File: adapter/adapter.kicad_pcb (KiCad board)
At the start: 2 copper layers, 41.8 x 50.8 mm, 28 parts, among them J1 Serial, J2 Battery charge, J3 Ribbon, J4 Ribbon, J5 RGB, SW1 SW_SPST, SW3 SW_SPDT, U1 Dual MCU: RP2040 + nice!nano, U2 AP1603WG-7, U3 USBLC6-2P6

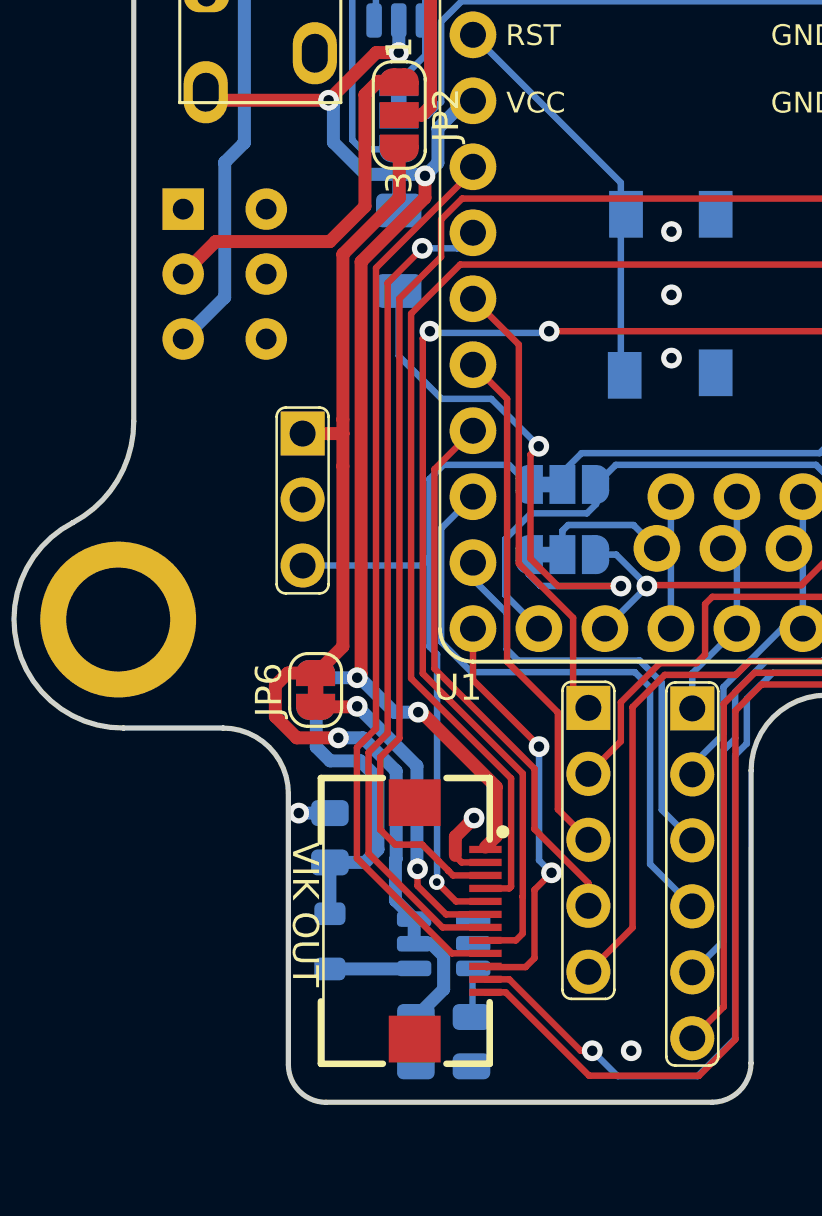
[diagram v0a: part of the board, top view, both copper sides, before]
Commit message: pcb: update silk screen to have text
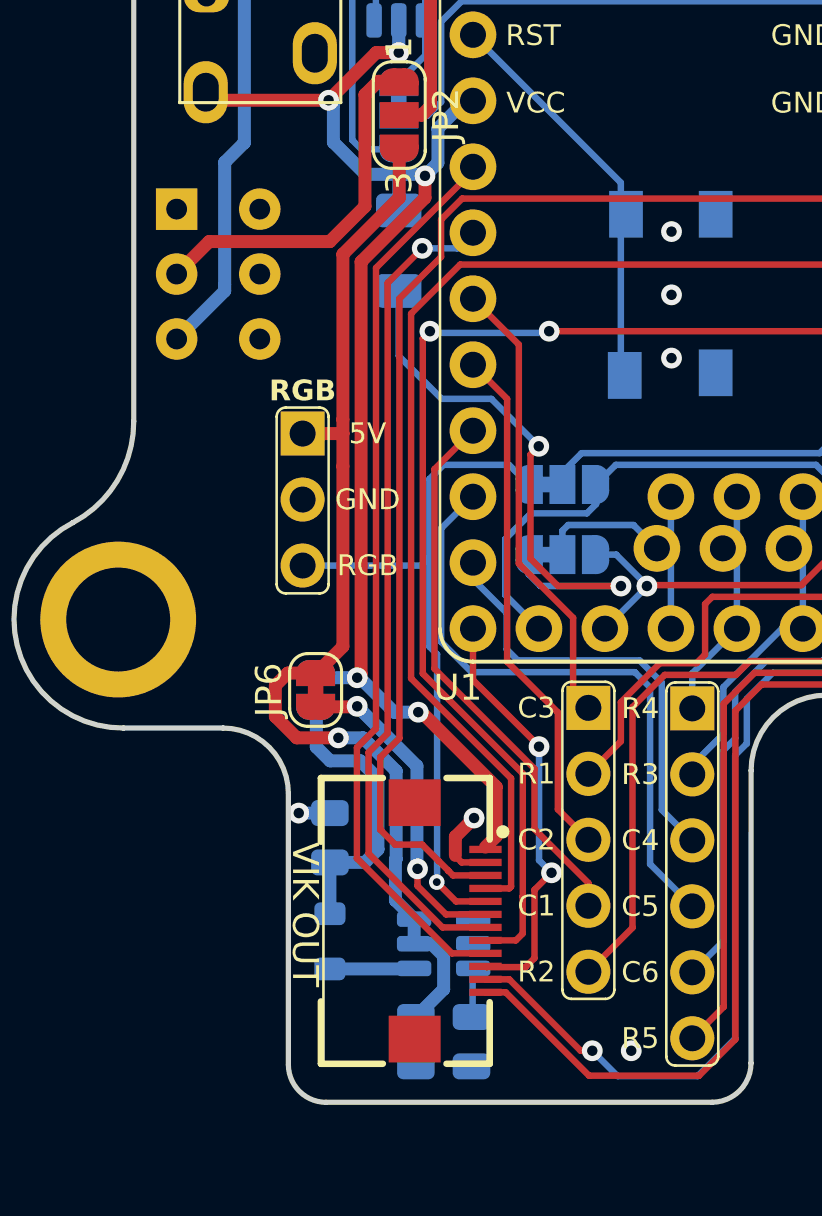
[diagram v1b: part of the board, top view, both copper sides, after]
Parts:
- moved SW3 0.25 mm to (119.2, 83.6)
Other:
- board text removed: "5V"
- board text removed: "DIN"
- board text removed: "GND"

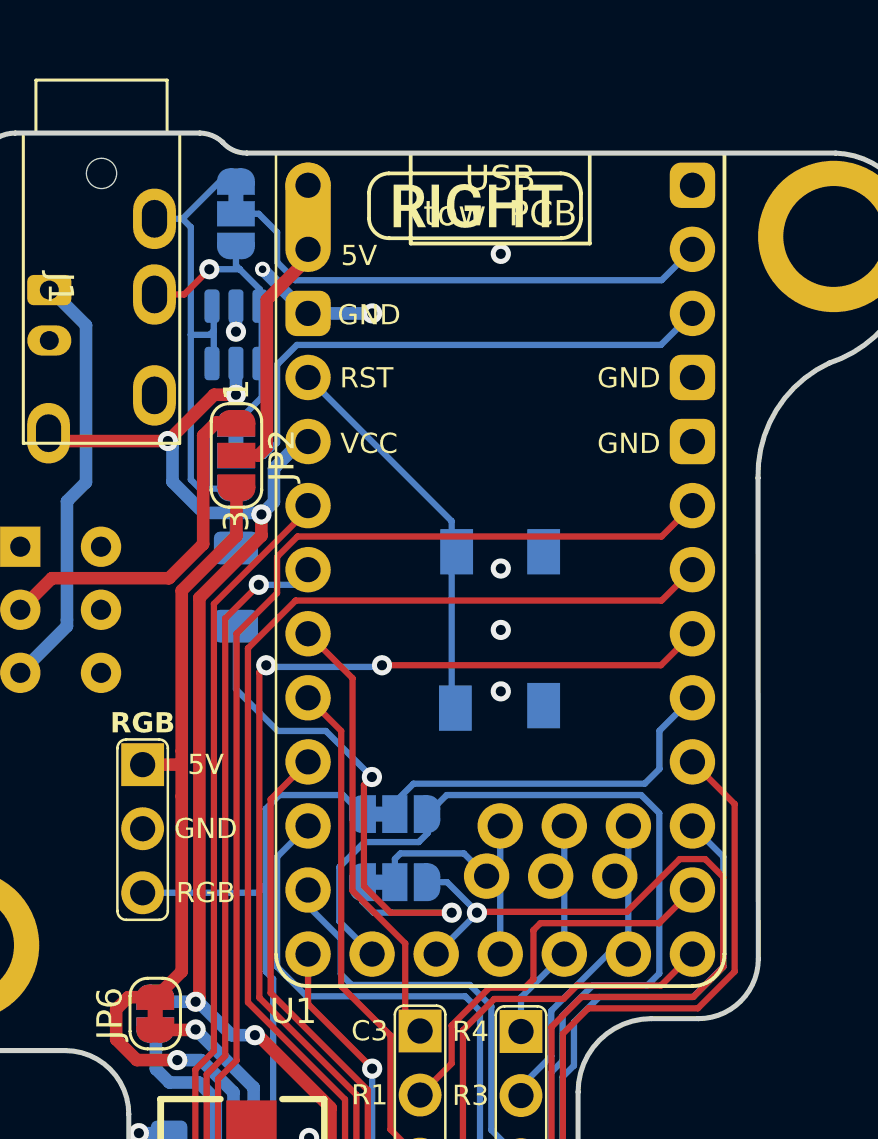
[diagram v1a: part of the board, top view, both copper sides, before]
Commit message: pcb: update silk screen on mcus
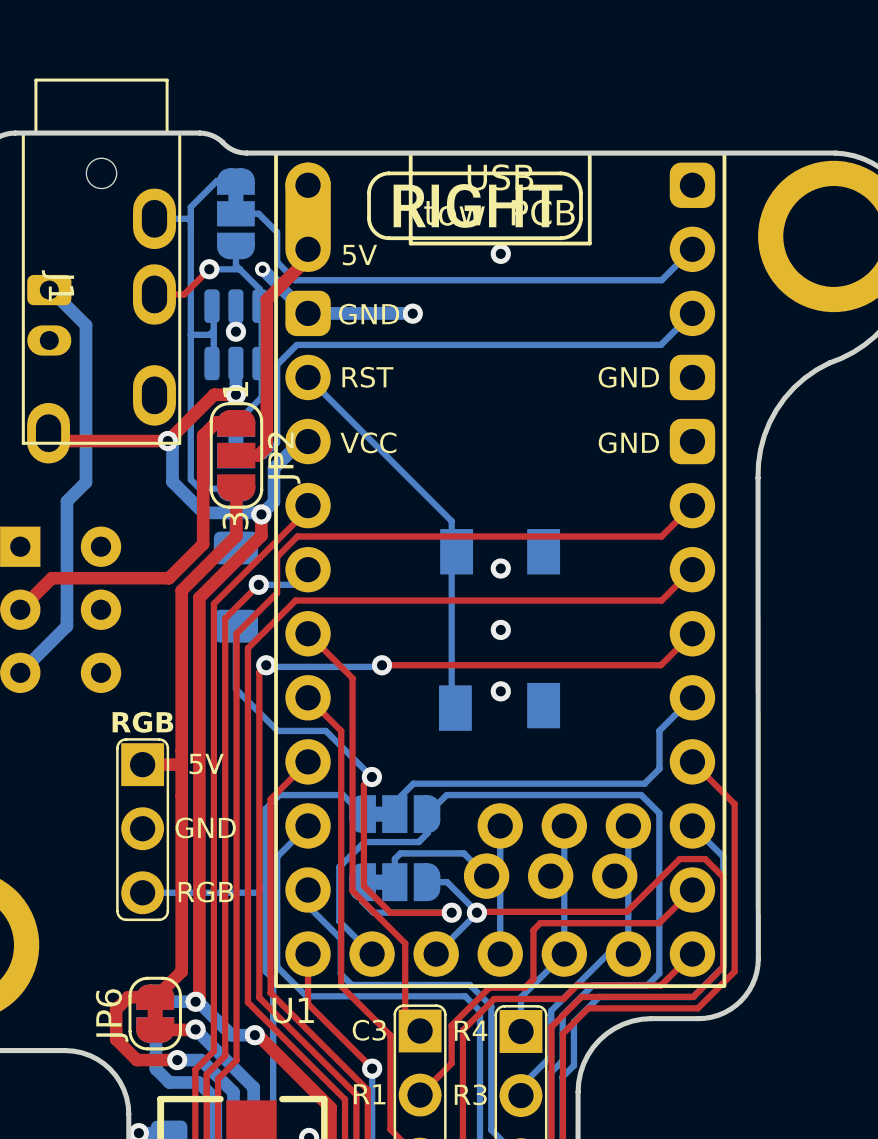
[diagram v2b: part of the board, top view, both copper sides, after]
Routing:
- net GND_L: track 10.3 -> 12.0 mm
- net TX_L: track 19.1 -> 19.9 mm

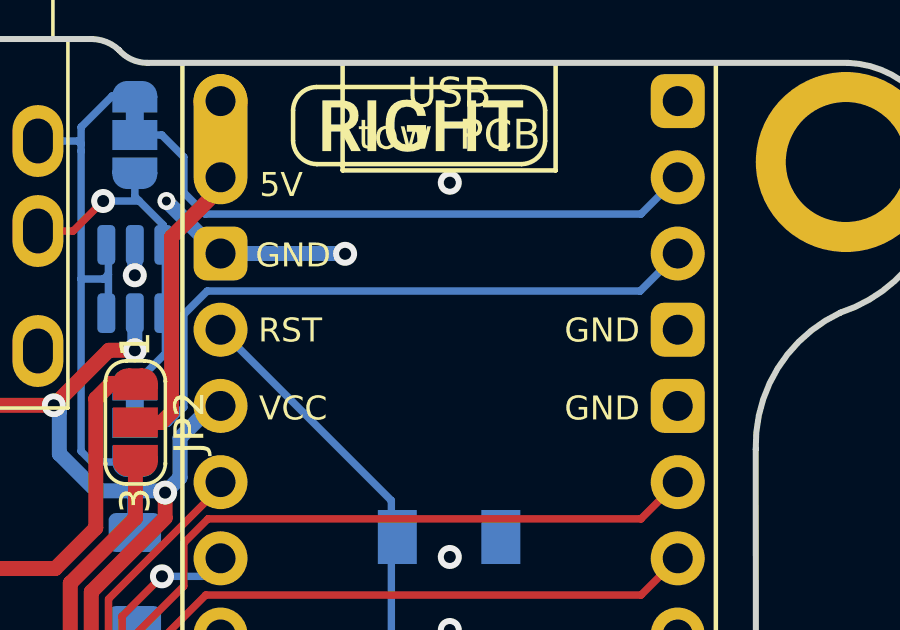
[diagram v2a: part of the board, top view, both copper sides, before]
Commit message: pcb: add osh silk screen
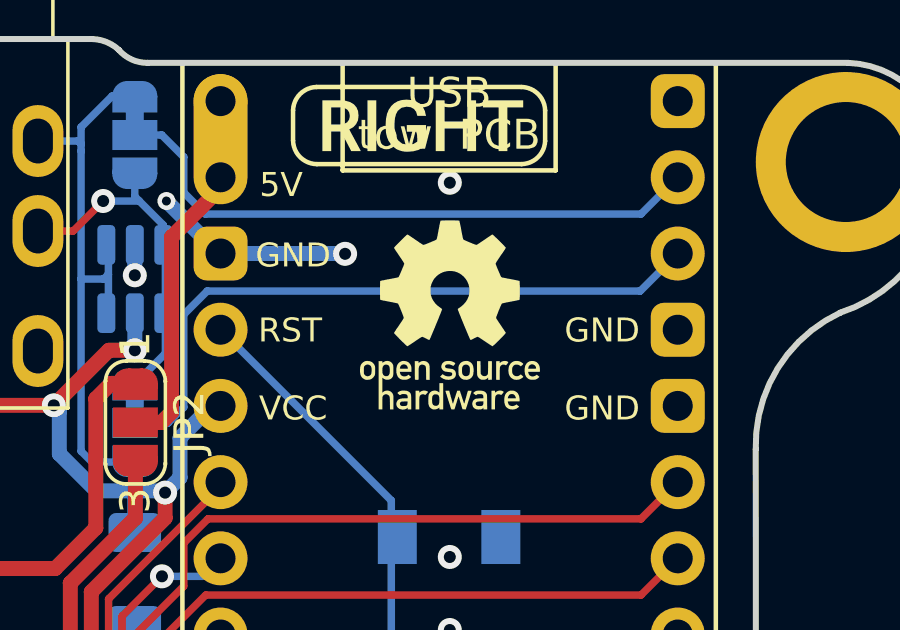
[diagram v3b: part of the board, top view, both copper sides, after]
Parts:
- added G***: LOGO, LOGO, F.Cu at (138.2, 76.4)
- added G***: LOGO, LOGO, B.Cu at (138.2, 76.4)

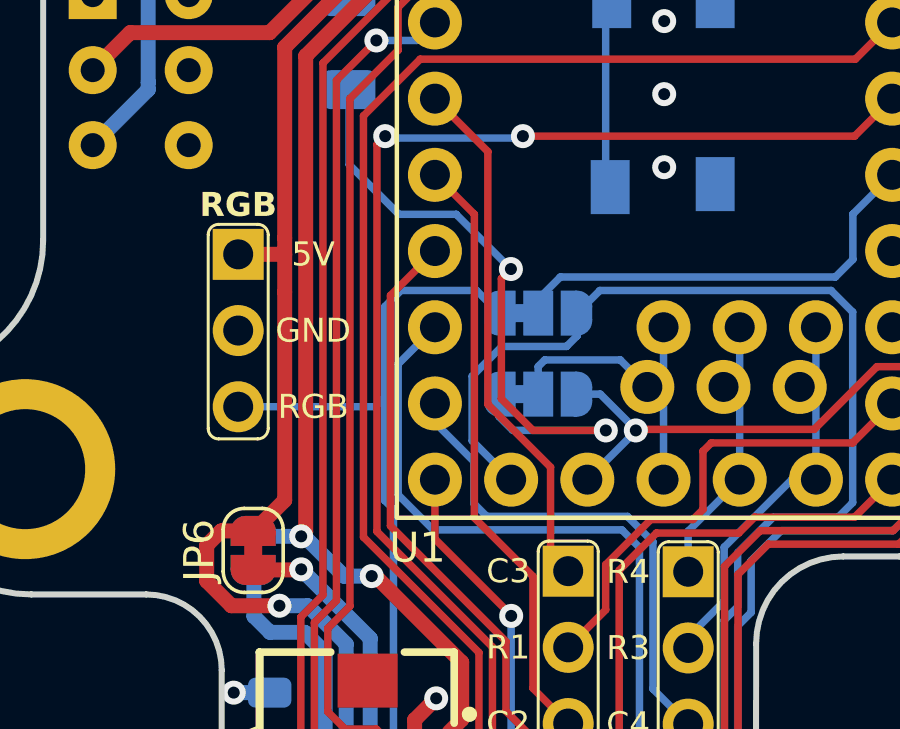
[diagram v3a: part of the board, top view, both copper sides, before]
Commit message: pcb: add more sikscreen
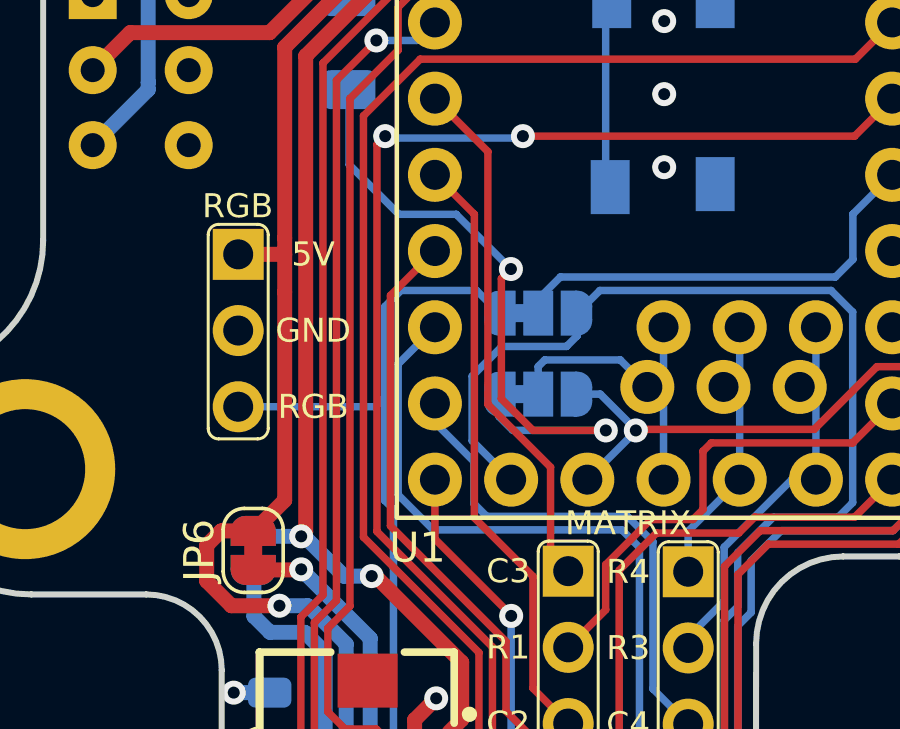
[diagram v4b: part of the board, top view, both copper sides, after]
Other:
- board text added: "MATRIX"

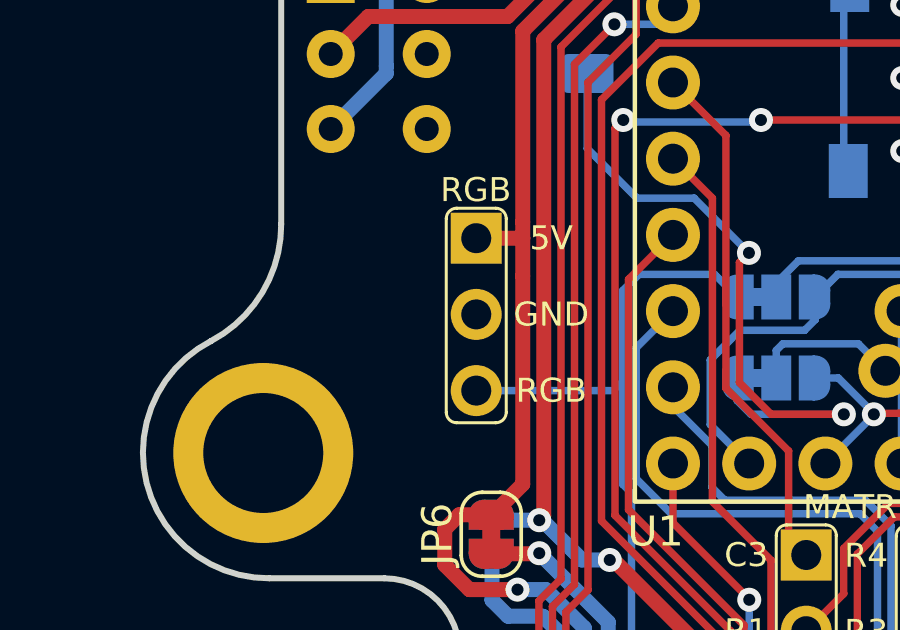
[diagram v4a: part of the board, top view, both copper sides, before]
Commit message: pcb: fix drc
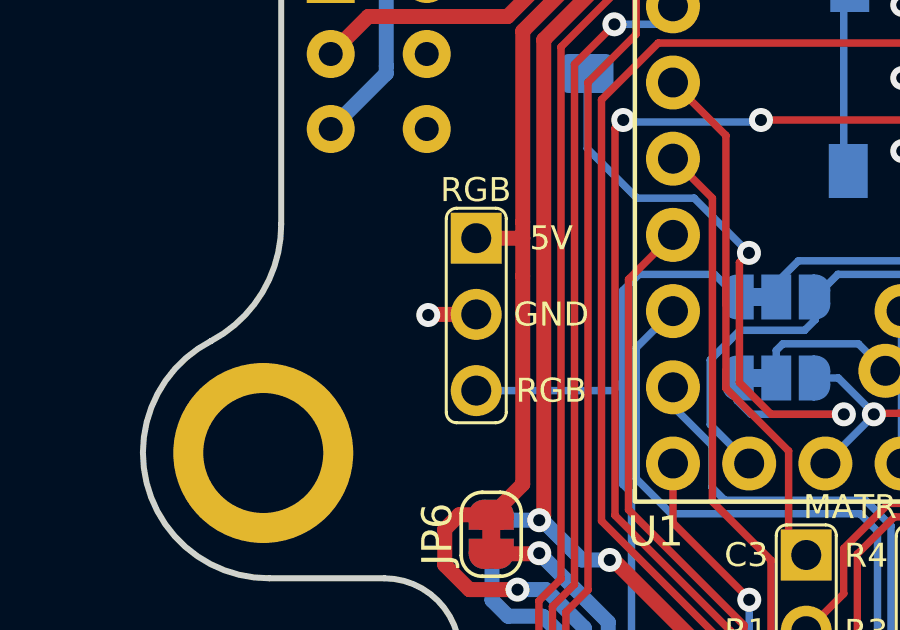
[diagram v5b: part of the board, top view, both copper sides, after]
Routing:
- net GND_L: track 12.0 -> 13.6 mm, vias 10 -> 11
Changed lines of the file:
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@@
 		(fp_arc
 			(start 1 10.852513)
-			(mid 0.897486 11.099999)
+			(mid 0.897486 11.099998)
 			(end 0.65 11.202513)
 			(stroke
@@
 		(fp_arc
 			(start 1 10.852513)
-			(mid 0.897486 11.099999)
+			(mid 0.897486 11.099998)
 			(end 0.65 11.202513)
 			(stroke
@@
 		(fp_arc
 			(start 1 5.802513)
-			(mid 0.897489 6.050002)
+			(mid 0.897489 6.050001)
 			(end 0.65 6.152513)
 			(stroke
@@
 		(fp_arc
 			(start 1 5.802513)
-			(mid 0.897489 6.050002)
+			(mid 0.897489 6.050001)
 			(end 0.65 6.152513)
 			(stroke
@@
 	)
 	(segment
+		(start 124 94.78)
+		(end 122.42 94.78)
+		(width 0.5)
+		(layer "F.Cu")
+		(net 12)
+	)
+	(segment
 		(start 128.753695 72.553333)
 		(end 128.814892 72.492136)
@@
 	)
 	(segment
+		(start 122.42 94.78)
+		(end 122.4 94.8)
+		(width 0.25)
+		(layer "F.Cu")
+		(net 12)
+	)
+	(segment
 		(start 129.88 107.76)
 		(end 130.6 107.04)
@@
 		(layers "F.Cu" "B.Cu")
 		(net 12)
+	)
+	(via
+		(at 122.4 94.8)
+		(size 0.8)
+		(drill 0.4)
+		(layers "F.Cu" "B.Cu")
+		(net 12)
